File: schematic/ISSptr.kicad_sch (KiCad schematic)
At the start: 0 parts

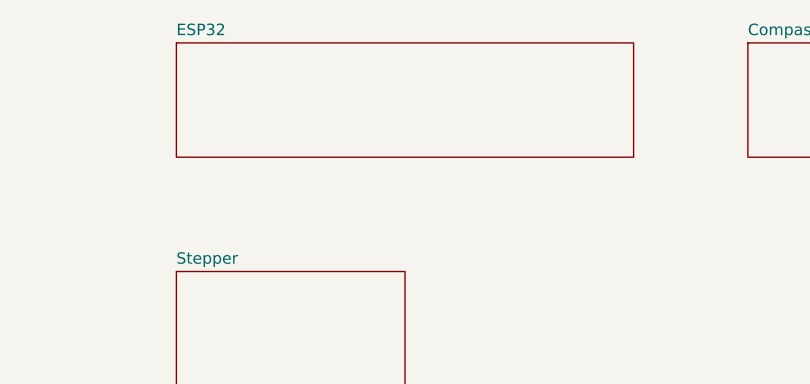
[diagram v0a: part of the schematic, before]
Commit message: Create ESP32 schematic
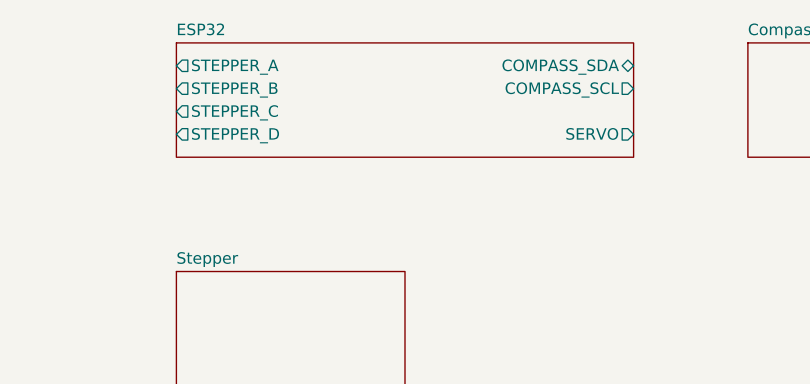
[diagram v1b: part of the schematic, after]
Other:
- sheet ESP32 ports: added COMPASS_SCL, COMPASS_SDA, SERVO, STEPPER_A, STEPPER_B, STEPPER_C, STEPPER_D; removed none
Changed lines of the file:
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@@
       (effects (font (size 1.27 1.27)) (justify left top) hide)
+    )
+    (pin "STEPPER_C" output (at 139.7 71.12 180)
+      (effects (font (size 1.27 1.27)) (justify left))
+    )
+    (pin "STEPPER_A" output (at 139.7 66.04 180)
+      (effects (font (size 1.27 1.27)) (justify left))
+    )
+    (pin "COMPASS_SDA" bidirectional (at 190.5 66.04 0)
+      (effects (font (size 1.27 1.27)) (justify right))
+    )
+    (pin "COMPASS_SCL" output (at 190.5 68.58 0)
+      (effects (font (size 1.27 1.27)) (justify right))
+    )
+    (pin "STEPPER_B" output (at 139.7 68.58 180)
+      (effects (font (size 1.27 1.27)) (justify left))
+    )
+    (pin "STEPPER_D" output (at 139.7 73.66 180)
+      (effects (font (size 1.27 1.27)) (justify left))
+    )
+    (pin "SERVO" output (at 190.5 73.66 0)
+      (effects (font (size 1.27 1.27)) (justify right))
     )
     (instances

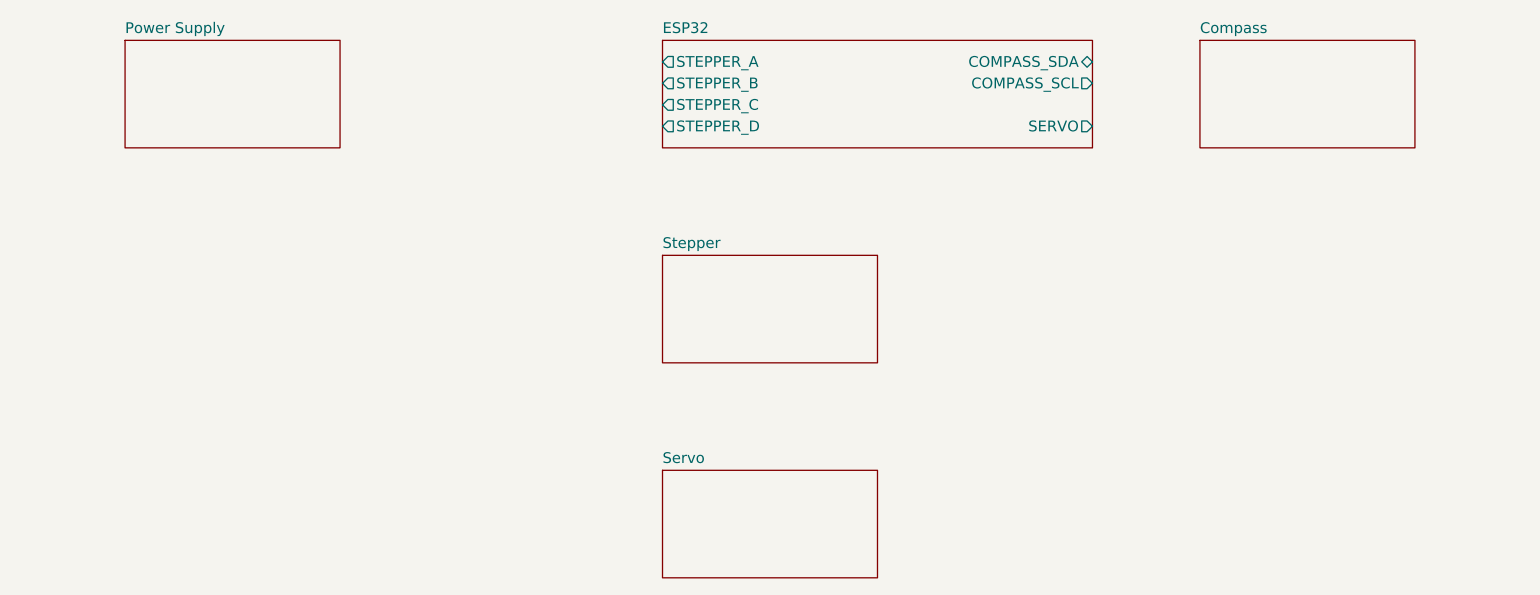
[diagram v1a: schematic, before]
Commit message: Create separator schematic
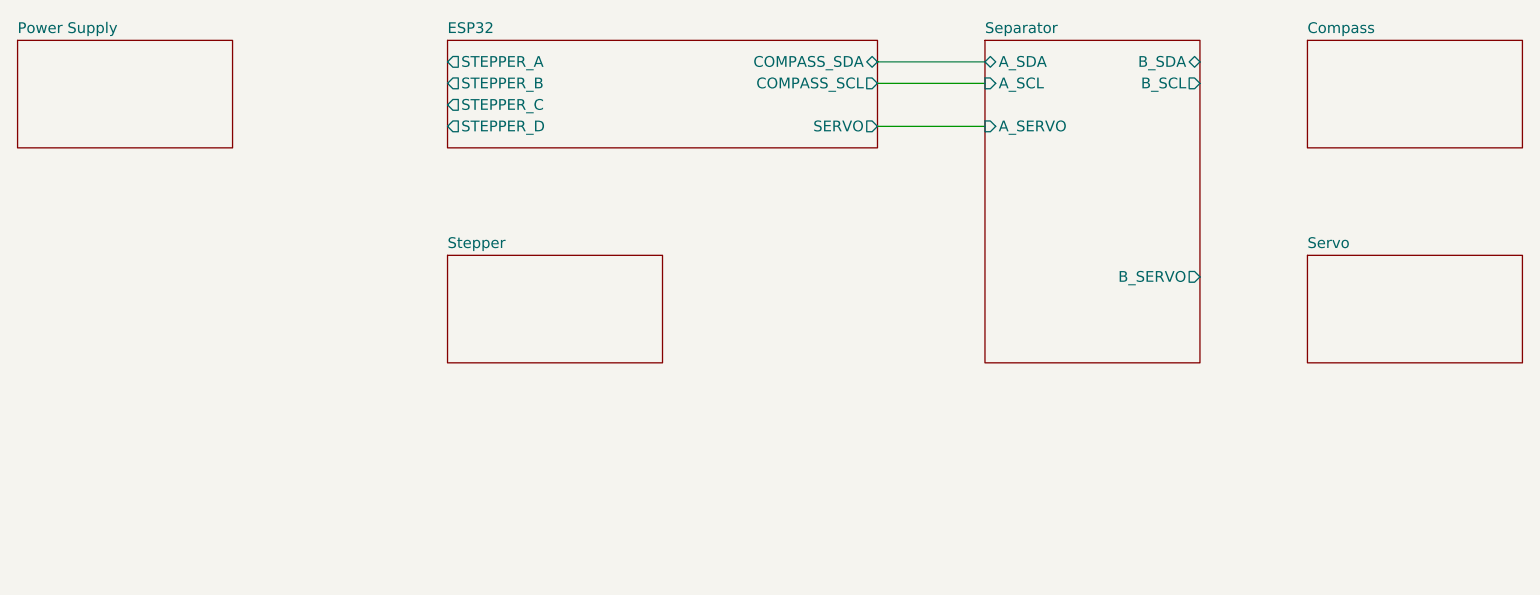
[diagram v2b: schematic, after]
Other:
- added sheet Separator (Separator.kicad_sch)
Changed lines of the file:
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@@
     (rev "v1")
   )
-  (sheet (at 203.2 63.5) (size 25.4 12.7) (fields_autoplaced)
+  (wire (pts (xy 165.1 68.58) (xy 177.8 68.58))
+    (stroke (width 0) (type default))
+  )
+  (wire (pts (xy 165.1 66.04) (xy 177.8 66.04))
+    (stroke (width 0) (type default))
+  )
+  (wire (pts (xy 165.1 73.66) (xy 177.8 73.66))
+    (stroke (width 0) (type default))
+  )
+  (sheet (at 215.9 63.5) (size 25.4 12.7) (fields_autoplaced)
     (stroke (width 0.1524) (type solid))
     (fill (color 0 0 0 0.0000))
-    (property "Sheetname" "Compass" (at 203.2 62.7884 0)
+    (property "Sheetname" "Compass" (at 215.9 62.7884 0)
       (effects (font (size 1.27 1.27)) (justify left bottom))
     )
-    (property "Sheetfile" "Compass.kicad_sch" (at 203.2 76.7846 0)
+    (property "Sheetfile" "Compass.kicad_sch" (at 215.9 76.7846 0)
       (effects (font (size 1.27 1.27)) (justify left top) hide)
     )
@@
     )
   )
-  (sheet (at 139.7 63.5) (size 50.8 12.7) (fields_autoplaced)
+  (sheet (at 114.3 63.5) (size 50.8 12.7) (fields_autoplaced)
     (stroke (width 0.1524) (type solid))
     (fill (color 0 0 0 0.0000))
-    (property "Sheetname" "ESP32" (at 139.7 62.7884 0)
+    (property "Sheetname" "ESP32" (at 114.3 62.7884 0)
       (effects (font (size 1.27 1.27)) (justify left bottom))
     )
-    (property "Sheetfile" "ESP32.kicad_sch" (at 139.7 76.7846 0)
+    (property "Sheetfile" "ESP32.kicad_sch" (at 114.3 76.7846 0)
       (effects (font (size 1.27 1.27)) (justify left top) hide)
     )
-    (pin "STEPPER_C" output (at 139.7 71.12 180)
+    (pin "STEPPER_C" output (at 114.3 71.12 180)
       (effects (font (size 1.27 1.27)) (justify left))
     )
-    (pin "STEPPER_A" output (at 139.7 66.04 180)
+    (pin "STEPPER_A" output (at 114.3 66.04 180)
       (effects (font (size 1.27 1.27)) (justify left))
     )
-    (pin "COMPASS_SDA" bidirectional (at 190.5 66.04 0)
+    (pin "COMPASS_SDA" bidirectional (at 165.1 66.04 0)
       (effects (font (size 1.27 1.27)) (justify right))
     )
-    (pin "COMPASS_SCL" output (at 190.5 68.58 0)
+    (pin "COMPASS_SCL" output (at 165.1 68.58 0)
       (effects (font (size 1.27 1.27)) (justify right))
     )
-    (pin "STEPPER_B" output (at 139.7 68.58 180)
+    (pin "STEPPER_B" output (at 114.3 68.58 180)
       (effects (font (size 1.27 1.27)) (justify left))
     )
-    (pin "STEPPER_D" output (at 139.7 73.66 180)
+    (pin "STEPPER_D" output (at 114.3 73.66 180)
       (effects (font (size 1.27 1.27)) (justify left))
     )
-    (pin "SERVO" output (at 190.5 73.66 0)
+    (pin "SERVO" output (at 165.1 73.66 0)
       (effects (font (size 1.27 1.27)) (justify right))
     )
@@
     )
   )
-  (sheet (at 139.7 114.3) (size 25.4 12.7) (fields_autoplaced)
+  (sheet (at 215.9 88.9) (size 25.4 12.7) (fields_autoplaced)
     (stroke (width 0.1524) (type solid))
     (fill (color 0 0 0 0.0000))
-    (property "Sheetname" "Servo" (at 139.7 113.5884 0)
+    (property "Sheetname" "Servo" (at 215.9 88.1884 0)
       (effects (font (size 1.27 1.27)) (justify left bottom))
     )
-    (property "Sheetfile" "Servo.kicad_sch" (at 139.7 127.5846 0)
+    (property "Sheetfile" "Servo.kicad_sch" (at 215.9 102.1846 0)
       (effects (font (size 1.27 1.27)) (justify left top) hide)
     )
@@
     )
   )
-  (sheet (at 76.2 63.5) (size 25.4 12.7) (fields_autoplaced)
+  (sheet (at 63.5 63.5) (size 25.4 12.7) (fields_autoplaced)
     (stroke (width 0.1524) (type solid))
     (fill (color 0 0 0 0.0000))
-    (property "Sheetname" "Power Supply" (at 76.2 62.7884 0)
+    (property "Sheetname" "Power Supply" (at 63.5 62.7884 0)
       (effects (font (size 1.27 1.27)) (justify left bottom))
     )
-    (property "Sheetfile" "PowerSupply.kicad_sch" (at 76.2 76.7846 0)
+    (property "Sheetfile" "PowerSupply.kicad_sch" (at 63.5 76.7846 0)
       (effects (font (size 1.27 1.27)) (justify left top) hide)
     )
@@
     )
   )
-  (sheet (at 139.7 88.9) (size 25.4 12.7) (fields_autoplaced)
+  (sheet (at 114.3 88.9) (size 25.4 12.7) (fields_autoplaced)
     (stroke (width 0.1524) (type solid))
     (fill (color 0 0 0 0.0000))
-    (property "Sheetname" "Stepper" (at 139.7 88.1884 0)
+    (property "Sheetname" "Stepper" (at 114.3 88.1884 0)
       (effects (font (size 1.27 1.27)) (justify left bottom))
     )
-    (property "Sheetfile" "Stepper.kicad_sch" (at 139.7 102.1846 0)
+    (property "Sheetfile" "Stepper.kicad_sch" (at 114.3 102.1846 0)
       (effects (font (size 1.27 1.27)) (justify left top) hide)
     )
@@
       )
     )
+  )
+  (sheet (at 177.8 63.5) (size 25.4 38.1) (fields_autoplaced)
+    (stroke (width 0.1524) (type solid))
+    (fill (color 0 0 0 0.0000))
+    (property "Sheetname" "Separator" (at 177.8 62.7884 0)
+      (effects (font (size 1.27 1.27)) (justify left bottom))
+    )
+    (property "Sheetfile" "Separator.kicad_sch" (at 177.8 102.1846 0)
+      (effects (font (size 1.27 1.27)) (justify left top) hide)
+    )
+    (pin "A_SCL" input (at 177.8 68.58 180)
+      (effects (font (size 1.27 1.27)) (justify left))
+    )
+    (pin "A_SERVO" input (at 177.8 73.66 180)
+      (effects (font (size 1.27 1.27)) (justify left))
+    )
+    (pin "A_SDA" bidirectional (at 177.8 66.04 180)
+      (effects (font (size 1.27 1.27)) (justify left))
+    )
+    (pin "B_SCL" output (at 203.2 68.58 0)
+      (effects (font (size 1.27 1.27)) (justify right))
+    )
+    (pin "B_SERVO" output (at 203.2 91.44 0)
+      (effects (font (size 1.27 1.27)) (justify right))
+    )
+    (pin "B_SDA" bidirectional (at 203.2 66.04 0)
+      (effects (font (size 1.27 1.27)) (justify right))
+    )
+    (instances
+      (project "ISSptr"
+        (path "/c978750c-b285-44b2-8d41-37a456977bcd" (page "7"))
+      )
+    )

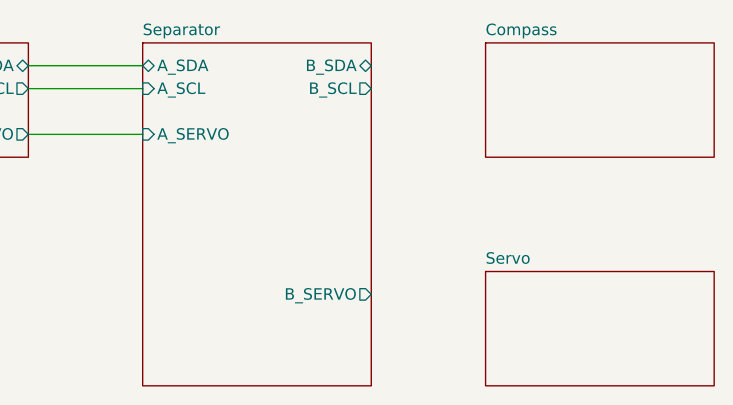
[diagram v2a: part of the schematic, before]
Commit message: Create compass schematic
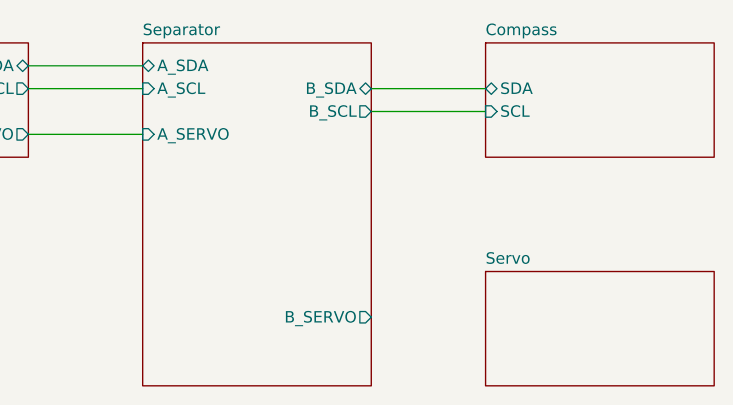
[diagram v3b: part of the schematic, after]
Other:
- sheet Compass ports: added SCL, SDA; removed none
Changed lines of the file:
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@@
     (rev "v1")
   )
+  (wire (pts (xy 203.2 68.58) (xy 215.9 68.58))
+    (stroke (width 0) (type default))
+  )
   (wire (pts (xy 165.1 68.58) (xy 177.8 68.58))
+    (stroke (width 0) (type default))
+  )
+  (wire (pts (xy 203.2 71.12) (xy 215.9 71.12))
     (stroke (width 0) (type default))
   )
@@
     (property "Sheetfile" "Compass.kicad_sch" (at 215.9 76.7846 0)
       (effects (font (size 1.27 1.27)) (justify left top) hide)
+    )
+    (pin "SDA" bidirectional (at 215.9 68.58 180)
+      (effects (font (size 1.27 1.27)) (justify left))
+    )
+    (pin "SCL" input (at 215.9 71.12 180)
+      (effects (font (size 1.27 1.27)) (justify left))
     )
     (instances
@@
       (effects (font (size 1.27 1.27)) (justify left))
     )
-    (pin "B_SCL" output (at 203.2 68.58 0)
+    (pin "B_SCL" output (at 203.2 71.12 0)
       (effects (font (size 1.27 1.27)) (justify right))
     )
-    (pin "B_SERVO" output (at 203.2 91.44 0)
+    (pin "B_SERVO" output (at 203.2 93.98 0)
       (effects (font (size 1.27 1.27)) (justify right))
     )
-    (pin "B_SDA" bidirectional (at 203.2 66.04 0)
+    (pin "B_SDA" bidirectional (at 203.2 68.58 0)
       (effects (font (size 1.27 1.27)) (justify right))
     )

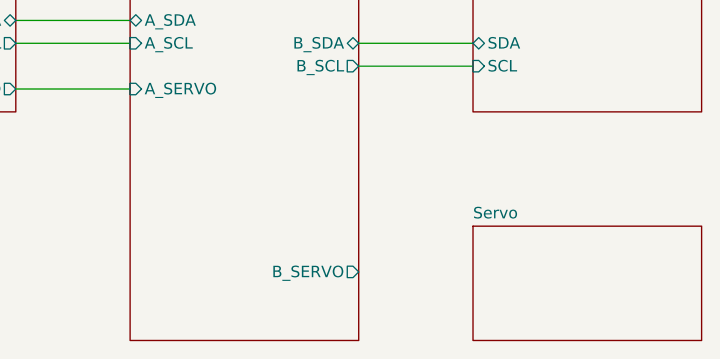
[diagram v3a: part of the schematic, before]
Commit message: Create servo header schematic
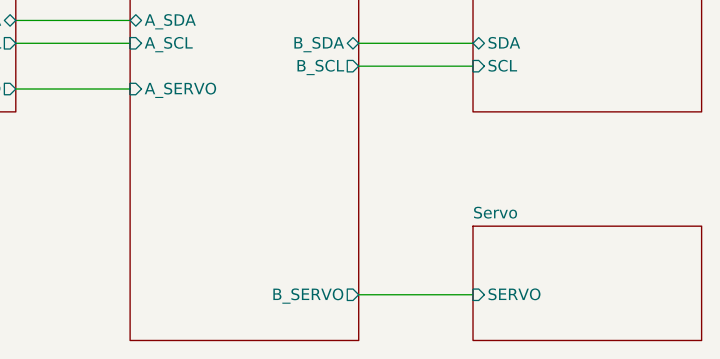
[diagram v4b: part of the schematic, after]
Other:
- sheet Servo ports: added SERVO; removed none
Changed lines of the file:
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@@
     (rev "v1")
+  )
+  (wire (pts (xy 203.2 96.52) (xy 215.9 96.52))
+    (stroke (width 0) (type default))
   )
   (wire (pts (xy 203.2 68.58) (xy 215.9 68.58))
@@
       (effects (font (size 1.27 1.27)) (justify left top) hide)
     )
+    (pin "SERVO" input (at 215.9 96.52 180)
+      (effects (font (size 1.27 1.27)) (justify left))
+    )
     (instances
       (project "ISSptr"
@@
       (effects (font (size 1.27 1.27)) (justify right))
     )
-    (pin "B_SERVO" output (at 203.2 93.98 0)
+    (pin "B_SERVO" output (at 203.2 96.52 0)
       (effects (font (size 1.27 1.27)) (justify right))
     )

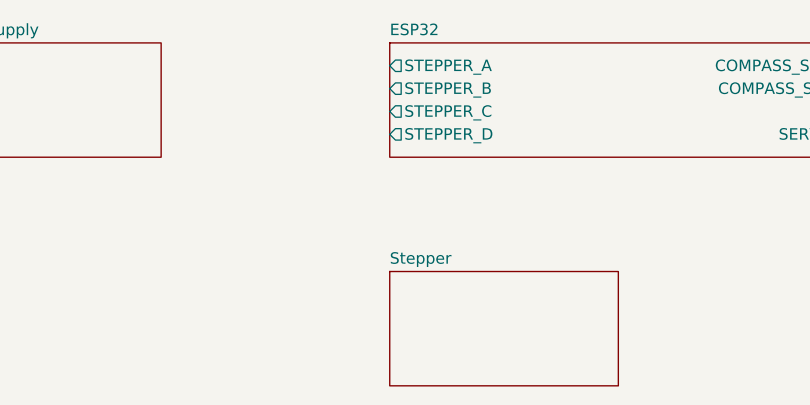
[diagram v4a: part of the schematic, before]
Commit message: Create stepper driver schematic
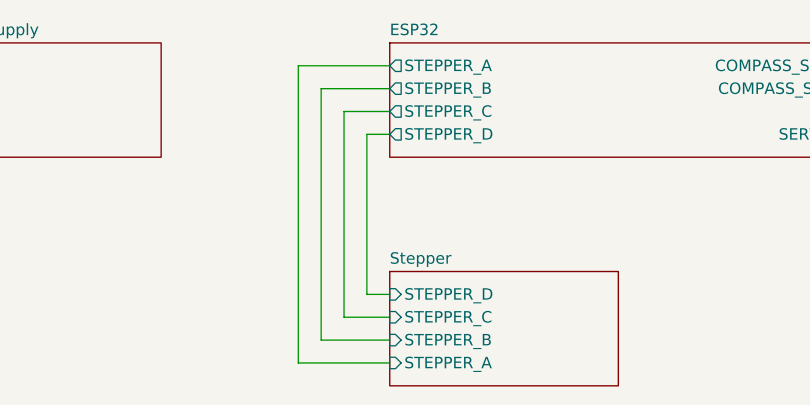
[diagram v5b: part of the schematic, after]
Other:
- sheet Stepper ports: added STEPPER_A, STEPPER_B, STEPPER_C, STEPPER_D; removed none
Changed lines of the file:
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@@
+    (stroke (width 0) (type default))
+  )
+  (wire (pts (xy 114.3 71.12) (xy 109.22 71.12))
     (stroke (width 0) (type default))
   )
@@
     (stroke (width 0) (type default))
   )
+  (wire (pts (xy 114.3 91.44) (xy 111.76 91.44))
+    (stroke (width 0) (type default))
+  )
+  (wire (pts (xy 104.14 66.04) (xy 104.14 99.06))
+    (stroke (width 0) (type default))
+  )
   (wire (pts (xy 165.1 68.58) (xy 177.8 68.58))
+    (stroke (width 0) (type default))
+  )
+  (wire (pts (xy 111.76 91.44) (xy 111.76 73.66))
     (stroke (width 0) (type default))
   )
@@
     (stroke (width 0) (type default))
   )
+  (wire (pts (xy 111.76 73.66) (xy 114.3 73.66))
+    (stroke (width 0) (type default))
+  )
+  (wire (pts (xy 104.14 99.06) (xy 114.3 99.06))
+    (stroke (width 0) (type default))
+  )
+  (wire (pts (xy 106.68 96.52) (xy 114.3 96.52))
+    (stroke (width 0) (type default))
+  )
+  (wire (pts (xy 114.3 66.04) (xy 104.14 66.04))
+    (stroke (width 0) (type default))
+  )
+  (wire (pts (xy 114.3 68.58) (xy 106.68 68.58))
+    (stroke (width 0) (type default))
+  )
   (wire (pts (xy 165.1 66.04) (xy 177.8 66.04))
     (stroke (width 0) (type default))
   )
+  (wire (pts (xy 106.68 68.58) (xy 106.68 96.52))
+    (stroke (width 0) (type default))
+  )
   (wire (pts (xy 165.1 73.66) (xy 177.8 73.66))
+    (stroke (width 0) (type default))
+  )
+  (wire (pts (xy 109.22 93.98) (xy 114.3 93.98))
+    (stroke (width 0) (type default))
+  )
+  (wire (pts (xy 109.22 71.12) (xy 109.22 93.98))
     (stroke (width 0) (type default))
   )
@@
       (effects (font (size 1.27 1.27)) (justify left top) hide)
     )
+    (pin "STEPPER_A" input (at 114.3 99.06 180)
+      (effects (font (size 1.27 1.27)) (justify left))
+    )
+    (pin "STEPPER_B" input (at 114.3 96.52 180)
+      (effects (font (size 1.27 1.27)) (justify left))
+    )
+    (pin "STEPPER_C" input (at 114.3 93.98 180)
+      (effects (font (size 1.27 1.27)) (justify left))
+    )
+    (pin "STEPPER_D" input (at 114.3 91.44 180)
+      (effects (font (size 1.27 1.27)) (justify left))
+    )
     (instances
